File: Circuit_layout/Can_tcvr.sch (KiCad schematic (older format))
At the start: 4 parts, among them U10 MCP2551-I/SN

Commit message: took notes w/ greg
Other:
- note added: "NOTE: DO NOT populate R11.\n\nR11 provides the ability to use this board \nas a terminating CAN node in development only."
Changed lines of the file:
@@
 Text Label 3000 1950 2    60   ~ 0
 CANRX
+Text Notes 4650 5050 0    60   ~ 0
+NOTE: DO NOT populate R11.\n\nR11 provides the ability to use this board \nas a terminating  CAN node in development only.
 $EndSCHEMATC

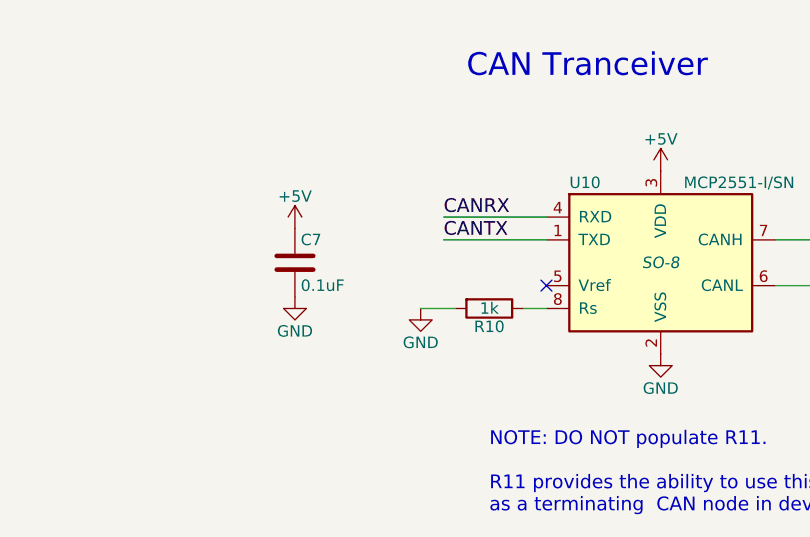
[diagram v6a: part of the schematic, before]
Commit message: added footprints
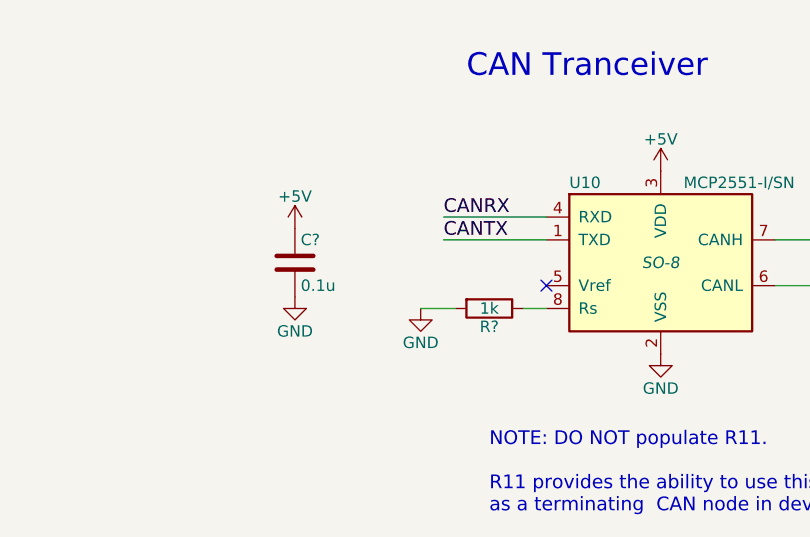
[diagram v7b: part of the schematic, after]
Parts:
- removed C7: 0.1uF, symbol C
- removed R10: 1k, symbol R
- added C?: 0.1u, Capacitors_SMD:C_0805_HandSoldering, symbol C
- added R?: 1k, Resistors_SMD:R_0805_HandSoldering, symbol R
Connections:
- net +5V: now also C?.1
- net GND: now also C?.2, R?.2
- net at U10.8 (Rs): now also R?.1
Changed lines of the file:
@@
 EESchema Schematic File Version 2
 LIBS:Circuit_layout-rescue
+LIBS:TSI_KiCad_Lib
 LIBS:TSI_HV_Isolater-cache
 LIBS:74xgxx
@@
 CANL
 $Comp
-L GND #PWR015
+L GND #PWR18
 U 1 1 58A63637
 P 5400 4350
-F 0 "#PWR015" H 5400 4100 50  0001 C CNN
+F 0 "#PWR18" H 5400 4100 50  0001 C CNN
 F 1 "GND" H 5400 4200 50  0000 C CNN
 F 2 "" H 5400 4350 50  0000 C CNN
@@
 $EndComp
 $Comp
-L GND #PWR016
+L GND #PWR16
 U 1 1 58A6364F
 P 4350 4150
-F 0 "#PWR016" H 4350 3900 50  0001 C CNN
+F 0 "#PWR16" H 4350 3900 50  0001 C CNN
 F 1 "GND" H 4350 4000 50  0000 C CNN
 F 2 "" H 4350 4150 50  0000 C CNN
@@
 	1    0    0    -1
 $EndComp
-$Comp
-L R R10
-U 1 1 58A63660
-P 4650 4150
-F 0 "R10" V 4730 4150 50  0000 C CNN
-F 1 "1k" V 4650 4150 50  0000 C CNN
-F 2 "" V 4580 4150 50  0000 C CNN
-F 3 "" H 4650 4150 50  0000 C CNN
-	1    4650 4150
-	0    1    1    0
-$EndComp
 Wire Wire Line
 	4500 4150 4350 4150
@@
 	4800 4150 4900 4150
 $Comp
-L +5V #PWR017
+L +5V #PWR17
 U 1 1 58A636CC
 P 5400 3550
-F 0 "#PWR017" H 5400 3400 50  0001 C CNN
+F 0 "#PWR17" H 5400 3400 50  0001 C CNN
 F 1 "+5V" H 5400 3690 50  0000 C CNN
 F 2 "" H 5400 3550 50  0000 C CNN
@@
 $EndComp
 $Comp
-L +5V #PWR018
+L +5V #PWR14
 U 1 1 58A636E7
 P 3800 3800
-F 0 "#PWR018" H 3800 3650 50  0001 C CNN
+F 0 "#PWR14" H 3800 3650 50  0001 C CNN
 F 1 "+5V" H 3800 3940 50  0000 C CNN
 F 2 "" H 3800 3800 50  0000 C CNN
@@
 $EndComp
 $Comp
-L GND #PWR019
+L GND #PWR15
 U 1 1 58A636FB
 P 3800 4100
-F 0 "#PWR019" H 3800 3850 50  0001 C CNN
+F 0 "#PWR15" H 3800 3850 50  0001 C CNN
 F 1 "GND" H 3800 3950 50  0000 C CNN
 F 2 "" H 3800 4100 50  0000 C CNN
 F 3 "" H 3800 4100 50  0000 C CNN
 	1    3800 4100
-	1    0    0    -1
-$EndComp
-$Comp
-L C C7
-U 1 1 58A6370E
-P 3800 3950
-F 0 "C7" H 3825 4050 50  0000 L CNN
-F 1 "0.1uF" H 3825 3850 50  0000 L CNN
-F 2 "" H 3838 3800 50  0000 C CNN
-F 3 "" H 3800 3950 50  0000 C CNN
-	1    3800 3950
 	1    0    0    -1
 $EndComp
@@
 Text Notes 4650 5050 0    60   ~ 0
 NOTE: DO NOT populate R11.\n\nR11 provides the ability to use this board \nas a terminating  CAN node in development only.
+$Comp
+L C C?
+U 1 1 58B93C80
+P 3800 3950
+F 0 "C?" H 3825 4050 50  0000 L CNN
+F 1 "0.1u" H 3825 3850 50  0000 L CNN
+F 2 "Capacitors_SMD:C_0805_HandSoldering" H 3838 3800 50  0001 C CNN
+F 3 "http://www.kemet.com/Lists/ProductCatalog/Attachments/53/KEM_C1002_X7R_SMD.pdf" H 3800 3950 50  0001 C CNN
+F 4 "399-1168-1-ND" H 3800 3950 60  0001 C CNN "Digikey P/N"
+F 5 "http://www.digikey.com/product-detail/en/kemet/C0805C104K3RACTU/399-1168-1-ND/411443" H 3800 3950 60  0001 C CNN "URL"
+F 6 "C0805C104K3RACTU" H 3800 3950 60  0001 C CNN "Man P/N"
+	1    3800 3950
+	1    0    0    -1
+$EndComp
+$Comp
+L R R?
+U 1 1 58B983FD
+P 4650 4150
+F 0 "R?" V 4730 4150 50  0000 C CNN
+F 1 "1k" V 4650 4150 50  0000 C CNN
+F 2 "Resistors_SMD:R_0805_HandSoldering" V 4580 4150 50  0001 C CNN
+F 3 "" H 4650 4150 50  0000 C CNN
+F 4 "P1.00KCCT-ND" V 4650 4150 60  0001 C CNN "DigiKey P/N"
+F 5 "http://www.digikey.com/product-detail/en/panasonic-electronic-components/ERJ-6ENF1001V/P1.00KCCT-ND/118957" V 4650 4150 60  0001 C CNN "URL"
+F 6 "ERJ-6ENF1001V" V 4650 4150 60  0001 C CNN "Man P/N"
+	1    4650 4150
+	0    1    1    0
+$EndComp
 $EndSCHEMATC
